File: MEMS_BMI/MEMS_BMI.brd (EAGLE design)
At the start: 72.1 x 57.5 mm, 85 parts, among them J1 2x3p-2.54, J2 HR911105A, J5 2X10P-2.54, K1 botton, K2 B3U-1000P, Q1 CSM-7X-DU, U1 AMS1117-3.3V, Y1 25MHZ

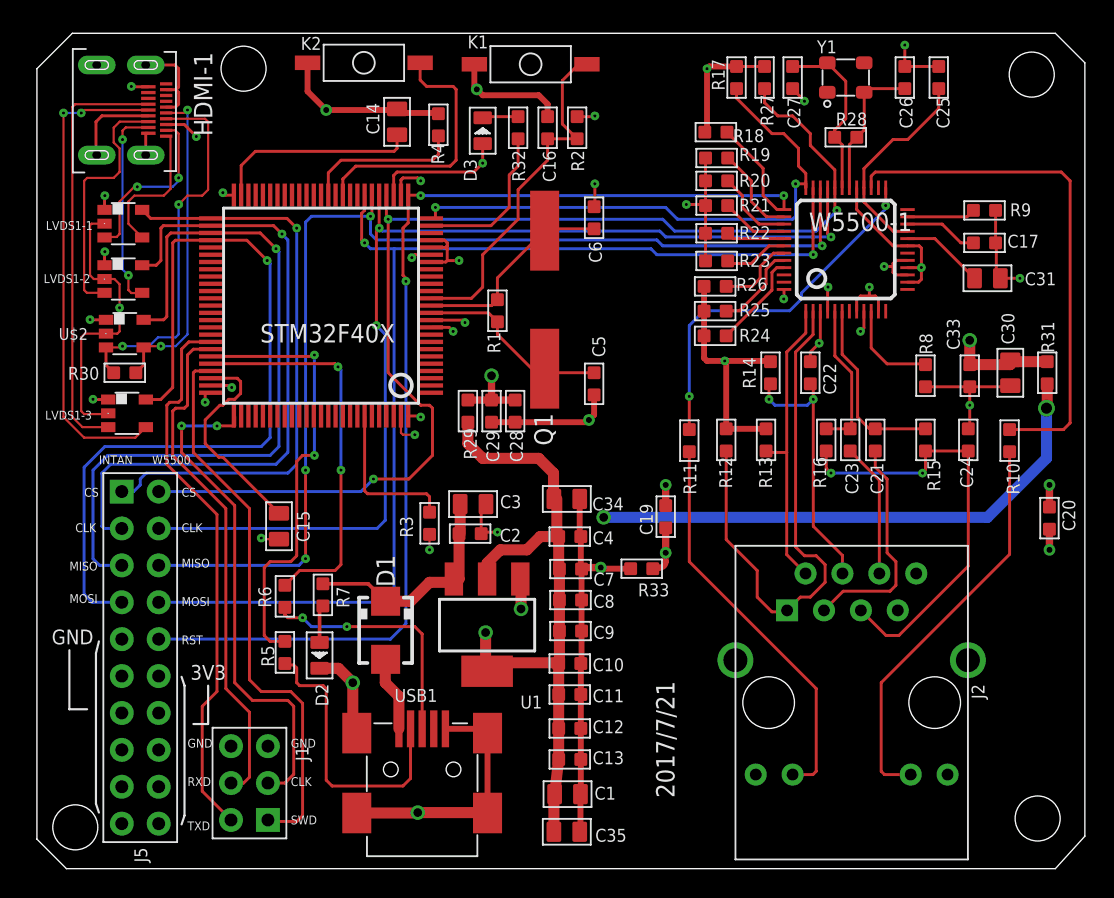
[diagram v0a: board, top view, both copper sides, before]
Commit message: intan added, BMI-V2
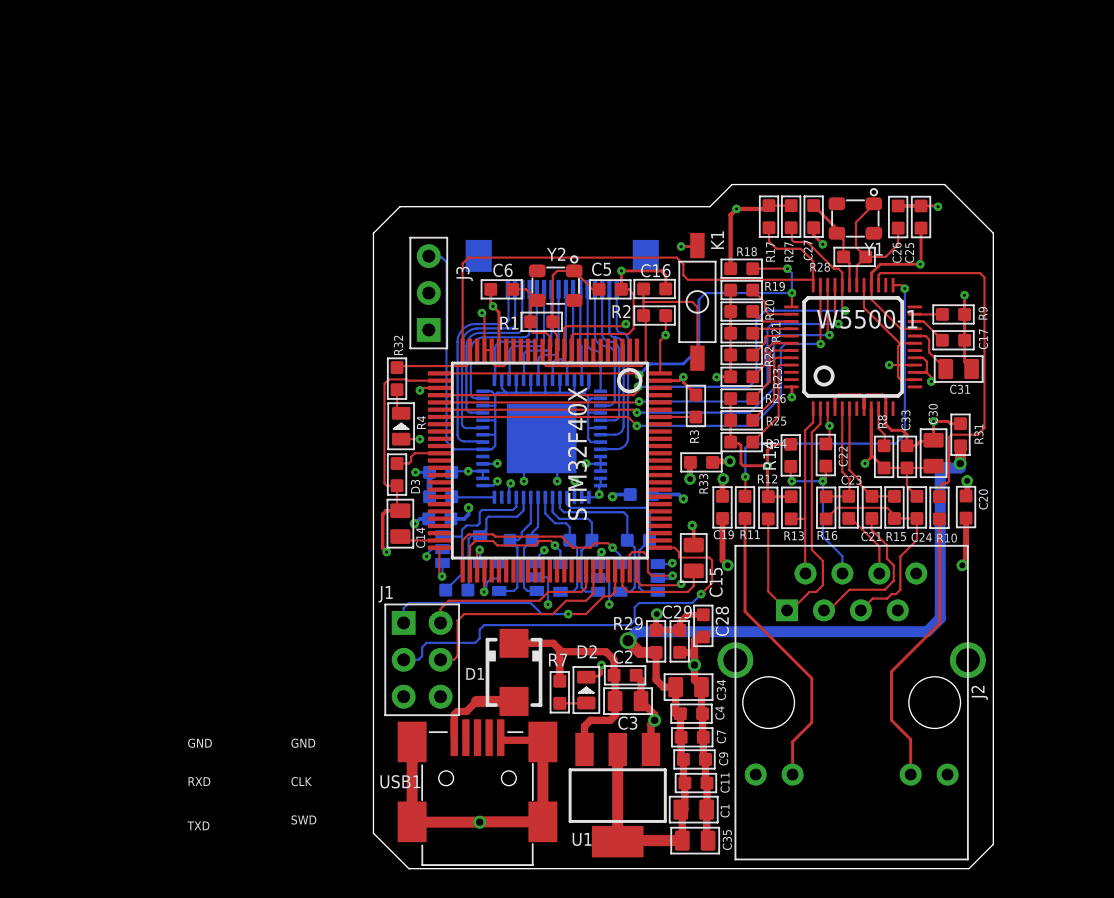
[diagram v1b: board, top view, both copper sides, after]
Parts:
- removed C10, C12, C13, C8: 104, 1-intan:C0603
- removed HDMI-1: MICRO-HDMI, 1-intan:HDMI
- removed J5: 2X10P-2.54, Seeed-OPL-Connector:H2X10-2.54
- removed K2: B3U-1000P, 1-intan:SW2-SMD-3.0X6.0*2.5
- removed Q1: CSM-7X-DU, crystal:CSM-7X-DU
- added C18: 10n, 1-intan:C0603
- added C32: 100n, 1-intan:C0603
- added J3: 3P-2.54, Seeed-OPL-Connector:H3-2.54
- added R34, R35, R36: 100, 1-intan:R0603
- added U$3: PROBE, 1-intan:PROBE-16-PIN
- added U2: RHD2216_QFN, RHD2000:QFN56_8_X_8_LARGE
- added Y2: 30MHZ, Seeed-OPL-Crystal-Oscillator:X4-SMD-3.2X2.5X0.7MM
- R5, R6: value 22R -> 0
- moved LVDS1-1 43.1 mm to (41.5, 20.0), flipped to the bottom
- moved LVDS1-2 37.5 mm to (37.3, 20.0), flipped to the bottom
- moved LVDS1-3 29.2 mm to (33.1, 20.1), flipped to the bottom
- moved C15 28.6 mm to (45.2, 21.4), turned to 0 degrees
- moved C14 27.7 mm to (25.0, 23.7)
- moved U$2 27.5 mm to (29.2, 22.0), flipped to the bottom, turned to 90 degrees
- moved R30 27.3 mm to (28.9, 19.2), flipped to the bottom, turned to 270 degrees
- moved R6 25.5 mm to (41.6, 25.8), flipped to the bottom, turned to 270 degrees
- moved R4 24.2 mm to (24.8, 27.1), turned to 180 degrees
- moved D3 21.1 mm to (25.1, 30.5)
- moved C29 20.5 mm to (44.2, 15.6)
- moved R29 20.5 mm to (42.6, 15.6)
- moved R3 20.0 mm to (45.4, 31.9), turned to 0 degrees
- moved K1 20.0 mm to (45.5, 39.0), turned to 270 degrees
- moved C28 19.7 mm to (45.9, 16.7)
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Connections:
- removed net N$2: R5.1, USB1.2
- removed net N$29: K2.2, U$1.35
- removed net N$3: R6.1, USB1.3
- removed net PA11/USB_DM: R5.2, U$1.70
- removed net PA12/USB_DP: R6.2, U$1.71
- new net CH0: U$3.P$16, U2.9
- new net CH1: U$3.P$15, U2.7
- new net CH12: U$3.P$4, U2.41
- new net CH13: U$3.P$3, U2.39
- new net CH14: U$3.P$2, U2.37
- new net CH15: U$3.P$1, U2.35
- new net CH2: U$3.P$14, U2.5
- new net CH3: U$3.P$13, U2.3
- new net CH4: U$3.P$12, U2.1
- new net N$30: C18.2, U2.28
- new net N$36: J3.3, U2.2, U2.34, U2.36, U2.38, U2.4, U2.40, U2.42, U2.44, U2.46, U2.48, U2.50, U2.52, U2.54, U2.56, U2.6, U2.8
- new net N$37: U$3.P$11, U2.55
- new net N$38: U$3.P$10, U2.53
- new net N$39: U$3.P$9, U2.51
- new net N$40: U$3.P$8, U2.49
- new net N$41: U$3.P$7, U2.47
- new net N$42: U$3.P$6, U2.45
- new net N$43: U$3.P$5, U2.43
- net +3V3: no longer C10.1, C12.1, C13.1, C8.1, J5.11, J5.12, J5.13, J5.14, J5.15
- net CLK+: now also R35.2, U2.21; no longer HDMI-1.4
- net CLK-: now also R35.1, U2.20; no longer HDMI-1.6
- net CS+: now also R34.2, U2.19; no longer HDMI-1.1
- net CS-: now also R34.1, U2.18; no longer HDMI-1.3
- net DVCC: now also C32.2, R5.1, R5.2, U2.13, U2.14, U2.15, U2.16, U2.26, U2.30, U2.31; no longer HDMI-1.18
- net GND: now also C18.1, C32.1, J3.1, J3.2, R6.1, R6.2, U2.10, U2.11, U2.12, U2.17, U2.29, U2.32, U2.CENTER; no longer C10.2, C12.2, C13.2, C8.2, HDMI-1.11, HDMI-1.17, HDMI-1.2, HDMI-1.5, HDMI-1.8, HDMI-1.P$1, HDMI-1.P$2, HDMI-1.P$3, HDMI-1.P$4, J5.10, J5.5, J5.6, J5.7, J5.8, J5.9, K2.1
- net MISO+: now also U2.25; no longer HDMI-1.7
- net MISO-: now also U2.24; no longer HDMI-1.9
- net MOSI+: now also R36.2, U2.23; no longer HDMI-1.10
- net MOSI-: now also R36.1, U2.22; no longer HDMI-1.12
- net N$19: now also Y1.3; no longer Y1.4
- net N$27: now also Y1.1; no longer Y1.2
- net OSC_IN: now also Y2.1; no longer Q1.2
- net OSC_OUT: now also Y2.3; no longer Q1.1
- net SPI2_CLK: no longer J5.2
- net SPI2_CS: no longer J5.1
- net SPI2_MISO: no longer J5.3
- net SPI2_MOSI: no longer J5.4
- net W5500_CLK: no longer J5.19
- net W5500_CS: no longer J5.20
- net W5500_MISO: no longer J5.18
- net W5500_MOSI: no longer J5.17
- net W5500_RST: no longer J5.16
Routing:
- net SPI2_MOSI: track 56.8 -> 4.13 mm
- net SPI2_MISO: track 50.7 -> 2.45 mm
- net W5500_RST: track 81.3 -> 33.8 mm
- net W5500_MOSI: track 79.5 -> 34.8 mm
- net N$36: track 0.00 -> 44.1 mm
- net W5500_MISO: track 76.3 -> 34.7 mm, vias 4 -> 2
- net W5500_CS: track 82.3 -> 40.9 mm, vias 3 -> 2
- net W5500_CLK: track 73.4 -> 34.7 mm, vias 3 -> 2
- net SPI2_CLK: track 46.0 -> 9.52 mm
- net PA11/USB_DM: track 30.8 -> 0.00 mm, vias 2 -> 0
- net PA12/USB_DP: track 27.0 -> 0.00 mm, vias 2 -> 0
- net SPI2_CS: track 40.5 -> 14.6 mm
- net TXD1: track 38.1 -> 12.7 mm
- net MOSI+: track 33.4 -> 8.69 mm, vias 2 -> 0
- net +3V3: track 86.3 -> 63.3 mm, vias 3 -> 2
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- removed copper zone on layer 3, net +3V3
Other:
- board size 72.1 x 57.5 mm -> 42.7 x 47.1 mm
- board text added: "BMI-V2"
- board text removed: "2017/7/21"
- board text removed: "3V3"
- board text removed: "BMI-V1"
- board text removed: "CS"
- board text removed: "INTAN"
- board text removed: "MISO"
- board text removed: "MOSI"
- board text removed: "RST"
- board text removed: "W5500"
